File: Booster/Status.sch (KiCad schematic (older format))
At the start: 41 parts

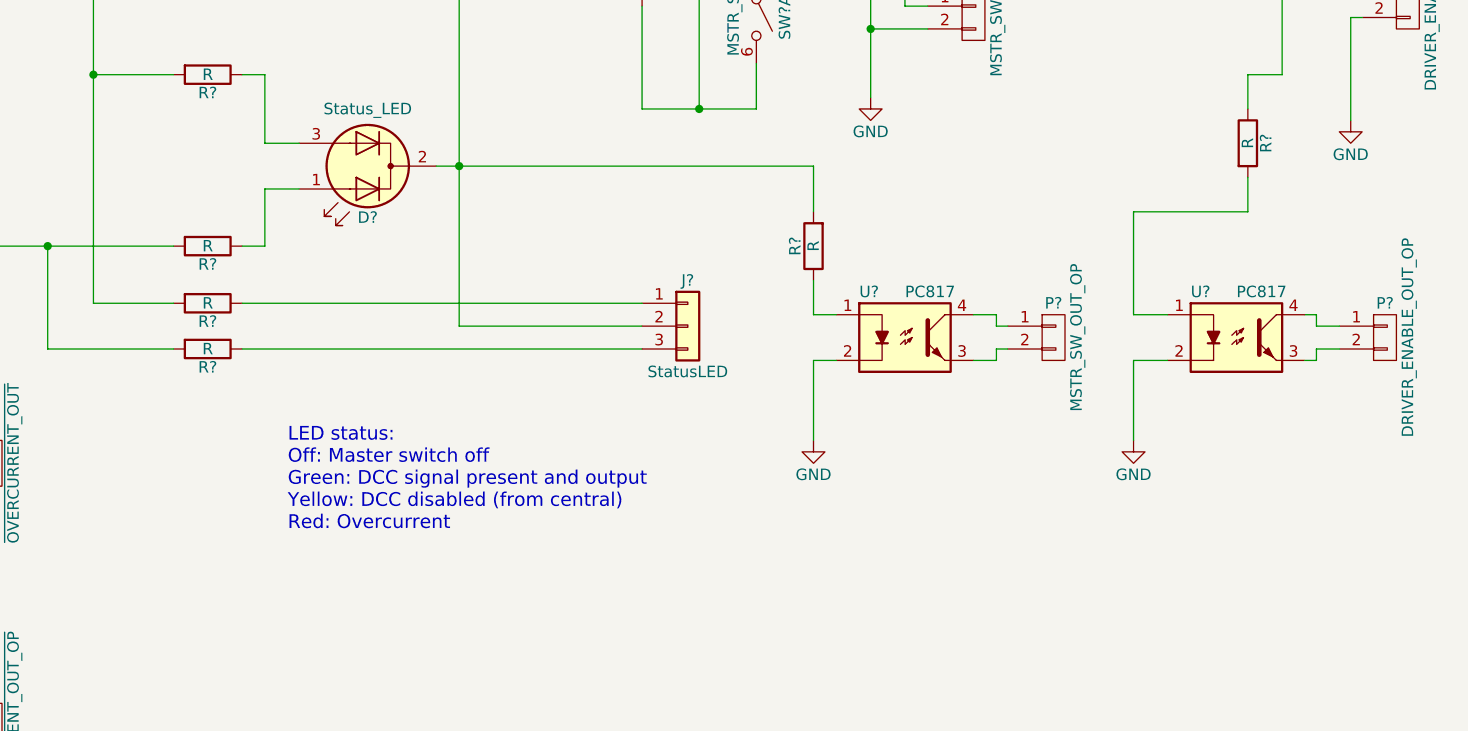
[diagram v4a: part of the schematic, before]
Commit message: Reset overcurrent timeout now linked to the master switch, not the input signal.
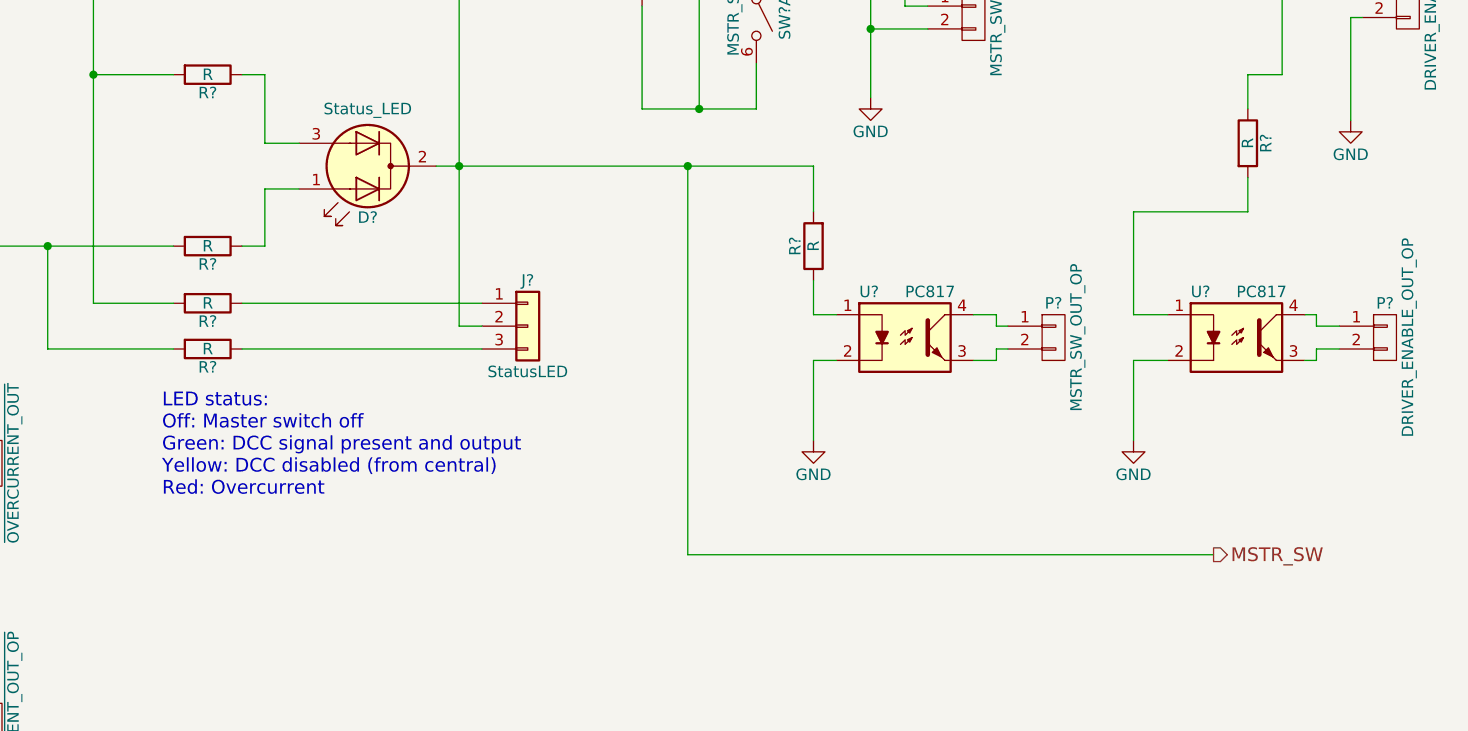
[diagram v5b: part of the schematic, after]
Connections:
- net MSTR_SW: now reaches D?.2 (K), J?.2 (Pin_2), P?.1 (P1), P?.1 (P1), R?.2, R?.2, SW?.1 (A), U?.13
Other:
- moved on the sheet: J?
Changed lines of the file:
@@
 Text HLabel 10250 2050 2    60   Output ~ 0
 DRIVER_ENABLE
-Text Notes 6050 5950 0    60   ~ 0
+Text Notes 5500 5800 0    60   ~ 0
 LED status:\nOff: Master switch off\nGreen: DCC signal present and output\nYellow: DCC disabled (from central)\nRed: Overcurrent
 $Comp
@@
 L Conn_01x03 J?
 U 1 1 5A0BF38D
-P 7800 5050
-F 0 "J?" H 7800 5250 50  0000 C CNN
-F 1 "StatusLED" H 7800 4850 50  0000 C CNN
-F 2 "" H 7800 5050 50  0001 C CNN
-F 3 "" H 7800 5050 50  0001 C CNN
-	1    7800 5050
+P 7100 5050
+F 0 "J?" H 7100 5250 50  0000 C CNN
+F 1 "StatusLED" H 7100 4850 50  0000 C CNN
+F 2 "" H 7100 5050 50  0001 C CNN
+F 3 "" H 7100 5050 50  0001 C CNN
+	1    7100 5050
 	1    0    0    -1
 $EndComp
@@
 	6700 4350 8350 4350
 Wire Wire Line
-	6800 5050 7600 5050
+	6800 5050 6900 5050
 Connection ~ 6800 4350
 Wire Wire Line
-	7600 4950 5850 4950
-Wire Wire Line
-	5850 5150 7600 5150
+	6900 4950 5850 4950
+Wire Wire Line
+	5850 5150 6900 5150
 Wire Wire Line
 	8100 3150 8100 3500
@@
 Text Notes 2300 3950 0    60   ~ 0
 Acting as inverter
+Wire Wire Line
+	7800 4350 7800 6050
+Wire Wire Line
+	7800 6050 10100 6050
+Connection ~ 7800 4350
+Text HLabel 10100 6050 2    60   Output ~ 0
+MSTR_SW
 $EndSCHEMATC

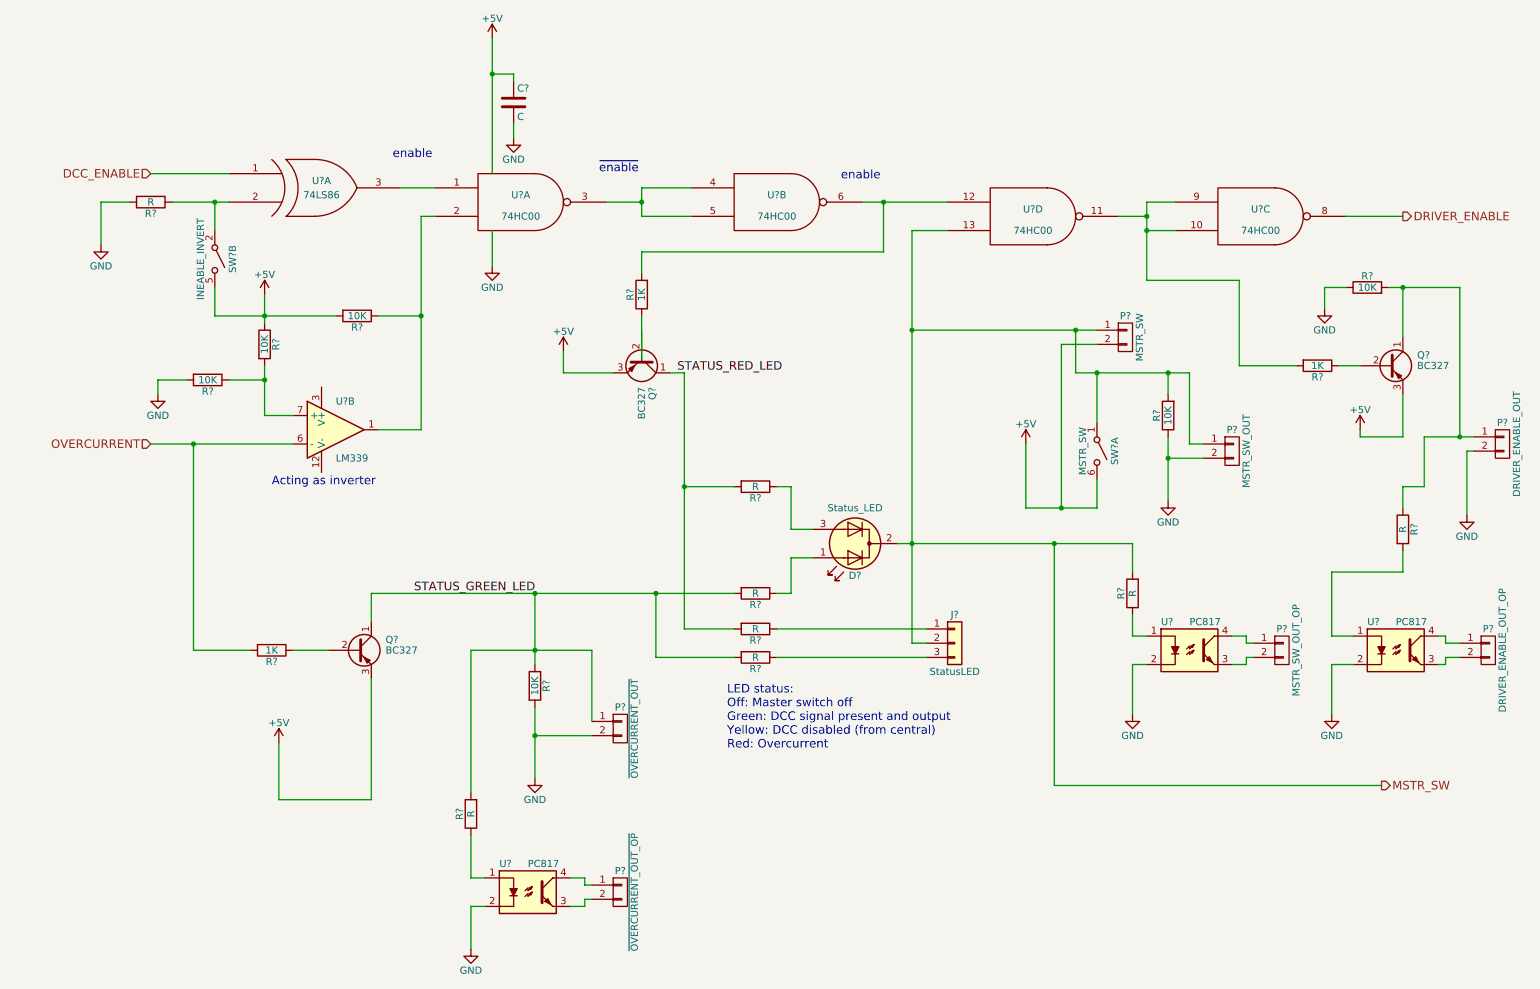
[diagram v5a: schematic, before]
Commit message: Removed need for enable signal replacing it with a missing pulse detection RC based circuit.
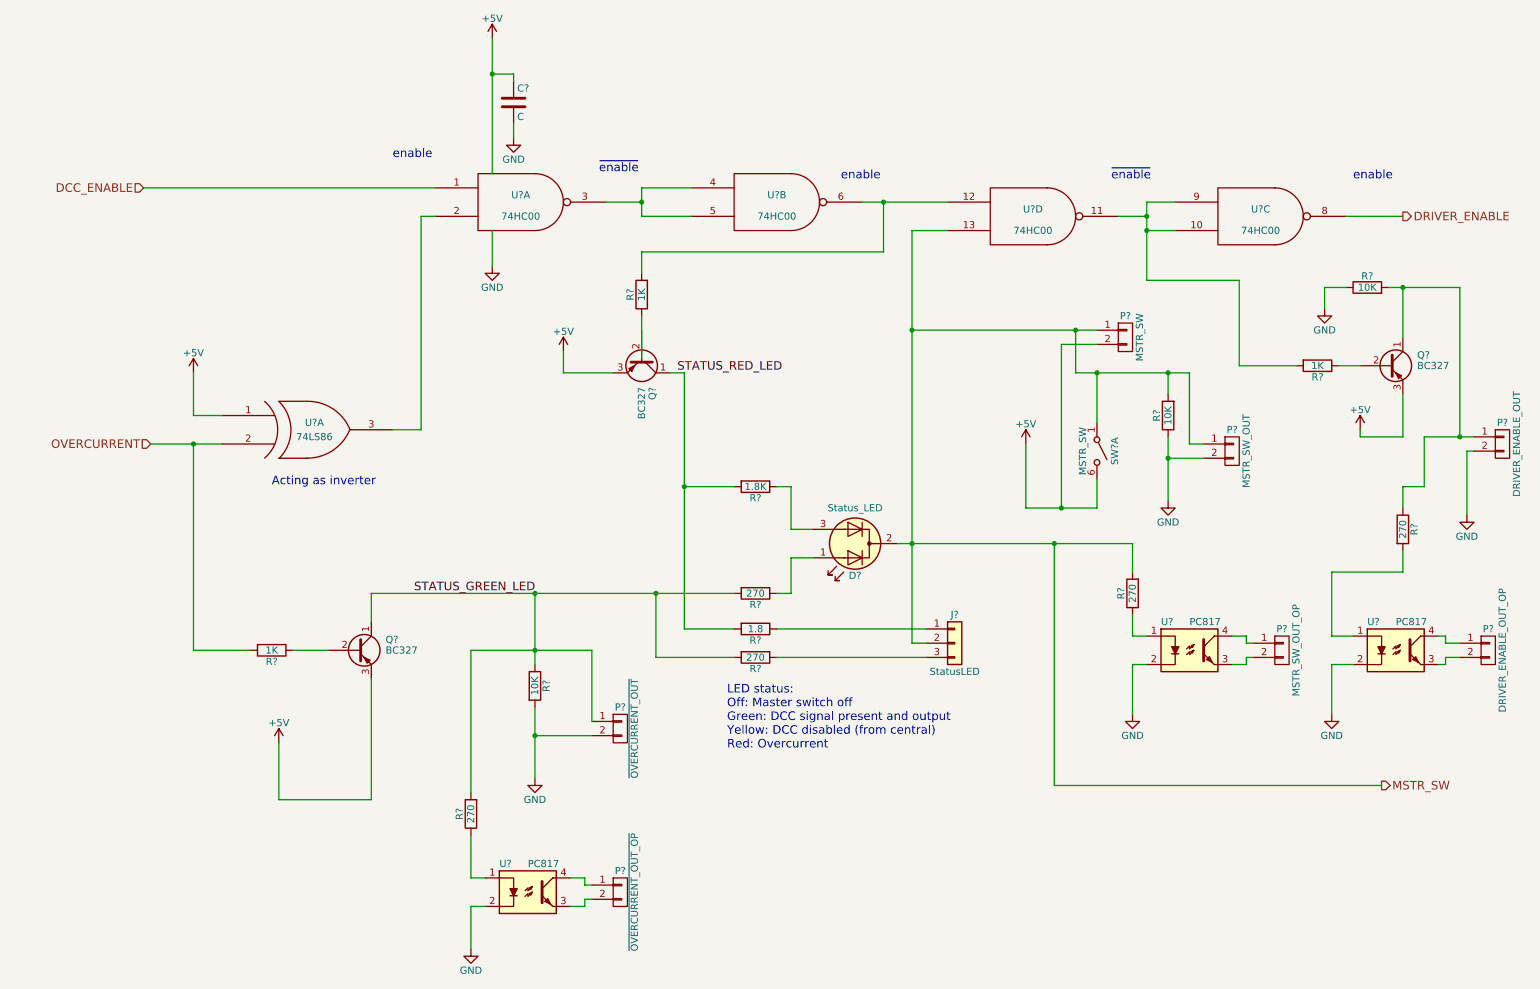
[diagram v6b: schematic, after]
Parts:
- removed R?: R, symbol R
- removed R? (x3): 10K, symbol R
- removed SW?: INEABLE_INVERT, symbol SW_SPST_x03
- removed U?: LM339, symbol LM339
- R? (x5): value R -> 270
- R?: value R -> 1.8K
- R?: value R -> 1.8
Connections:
- net +5V: now also U?.1 (IN1)
- net DCC_ENABLE: now also U?.1; no longer U?.1 (IN1)
- net OVERCURRENT: now also U?.2 (IN2)
- net at U?.3 (OUT): now also U?.2; no longer U?.1
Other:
- moved on the sheet: U?A
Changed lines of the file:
@@
 Comment4 ""
 $EndDescr
-Text HLabel 1450 1750 0    60   Input ~ 0
+Text HLabel 1400 1850 0    60   Input ~ 0
 DCC_ENABLE
 Text HLabel 1450 3650 0    60   Input ~ 0
@@
 P 5700 4700
 F 0 "R?" V 5780 4700 50  0000 C CNN
-F 1 "R" V 5700 4700 50  0000 C CNN
+F 1 "270" V 5700 4700 50  0000 C CNN
 F 2 "" V 5630 4700 50  0001 C CNN
 F 3 "" H 5700 4700 50  0001 C CNN
@@
 P 5700 3950
 F 0 "R?" V 5780 3950 50  0000 C CNN
-F 1 "R" V 5700 3950 50  0000 C CNN
+F 1 "1.8K" V 5700 3950 50  0000 C CNN
 F 2 "" V 5630 3950 50  0001 C CNN
 F 3 "" H 5700 3950 50  0001 C CNN
@@
 P 5700 4950
 F 0 "R?" V 5780 4950 50  0000 C CNN
-F 1 "R" V 5700 4950 50  0000 C CNN
+F 1 "1.8" V 5700 4950 50  0000 C CNN
 F 2 "" V 5630 4950 50  0001 C CNN
 F 3 "" H 5700 4950 50  0001 C CNN
@@
 P 5700 5150
 F 0 "R?" V 5780 5150 50  0000 C CNN
-F 1 "R" V 5700 5150 50  0000 C CNN
+F 1 "270" V 5700 5150 50  0000 C CNN
 F 2 "" V 5630 5150 50  0001 C CNN
 F 3 "" H 5700 5150 50  0001 C CNN
@@
 P 10250 4250
 F 0 "R?" V 10330 4250 50  0000 C CNN
-F 1 "R" V 10250 4250 50  0000 C CNN
+F 1 "270" V 10250 4250 50  0000 C CNN
 F 2 "" V 10180 4250 50  0001 C CNN
 F 3 "" H 10250 4250 50  0001 C CNN
@@
 P 8350 4700
 F 0 "R?" V 8430 4700 50  0000 C CNN
-F 1 "R" V 8350 4700 50  0000 C CNN
+F 1 "270" V 8350 4700 50  0000 C CNN
 F 2 "" V 8280 4700 50  0001 C CNN
 F 3 "" H 8350 4700 50  0001 C CNN
@@
 P 3700 6250
 F 0 "R?" V 3780 6250 50  0000 C CNN
-F 1 "R" V 3700 6250 50  0000 C CNN
+F 1 "270" V 3700 6250 50  0000 C CNN
 F 2 "" V 3630 6250 50  0001 C CNN
 F 3 "" H 3700 6250 50  0001 C CNN
@@
 L 74LS86 U?
 U 1 1 5A0F5EBC
-P 2600 1850
-F 0 "U?" H 2650 1900 50  0000 C CNN
-F 1 "74LS86" H 2650 1800 50  0000 C CNN
-F 2 "" H 2600 1850 50  0001 C CNN
-F 3 "" H 2600 1850 50  0001 C CNN
-	1    2600 1850
+P 2550 3550
+F 0 "U?" H 2600 3600 50  0000 C CNN
+F 1 "74LS86" H 2600 3500 50  0000 C CNN
+F 2 "" H 2550 3550 50  0001 C CNN
+F 3 "" H 2550 3550 50  0001 C CNN
+	1    2550 3550
 	1    0    0    -1
 $EndComp
@@
 $EndComp
 $Comp
-L SW_SPST_x03 SW?
-U 2 1 5A1166C8
-P 1900 2350
-F 0 "SW?" H 1900 2475 50  0000 C CNN
-F 1 "INEABLE_INVERT" H 1900 2250 50  0000 C CNN
-F 2 "" H 1900 2350 50  0001 C CNN
-F 3 "" H 1900 2350 50  0001 C CNN
-	2    1900 2350
-	0    1    1    0
-$EndComp
-$Comp
-L GND #PWR?
-U 1 1 5A116829
-P 1100 2250
-F 0 "#PWR?" H 1100 2000 50  0001 C CNN
-F 1 "GND" H 1100 2100 50  0000 C CNN
-F 2 "" H 1100 2250 50  0001 C CNN
-F 3 "" H 1100 2250 50  0001 C CNN
-	1    1100 2250
-	1    0    0    -1
-$EndComp
-$Comp
-L R R?
-U 1 1 5A116A16
-P 1450 1950
-F 0 "R?" V 1530 1950 50  0000 C CNN
-F 1 "R" V 1450 1950 50  0000 C CNN
-F 2 "" V 1380 1950 50  0001 C CNN
-F 3 "" H 1450 1950 50  0001 C CNN
-	1    1450 1950
-	0    1    1    0
-$EndComp
-$Comp
-L +5V #PWR?
-U 1 1 5A116BBB
-P 2250 2600
-F 0 "#PWR?" H 2250 2450 50  0001 C CNN
-F 1 "+5V" H 2250 2740 50  0000 C CNN
-F 2 "" H 2250 2600 50  0001 C CNN
-F 3 "" H 2250 2600 50  0001 C CNN
-	1    2250 2600
-	1    0    0    -1
-$EndComp
-$Comp
 L 74HC00 U?
 U 2 1 5A11F087
@@
 $EndComp
 Wire Wire Line
-	1450 1750 2000 1750
-Wire Wire Line
 	1750 3650 1750 5100
 Wire Wire Line
@@
 	3350 2050 3450 2050
 Wire Wire Line
-	3200 1850 3450 1850
-Wire Wire Line
 	4650 1950 4900 1950
 Wire Wire Line
@@
 	9850 2050 10250 2050
 Wire Wire Line
-	1600 1950 2000 1950
-Wire Wire Line
-	1300 1950 1100 1950
-Wire Wire Line
-	1100 1950 1100 2250
-Wire Wire Line
-	1900 2150 1900 1950
-Connection ~ 1900 1950
-Wire Wire Line
-	1900 2550 1900 2750
-Wire Wire Line
-	1900 2750 2750 2750
-Wire Wire Line
-	2250 2600 2250 2800
-Wire Wire Line
 	3850 2150 3850 2400
 Wire Wire Line
@@
 	6600 2300 6600 1950
 Connection ~ 6600 1950
-$Comp
-L LM339 U?
-U 2 1 5A375C9A
-P 2750 3550
-F 0 "U?" H 2750 3750 50  0000 L CNN
-F 1 "LM339" H 2750 3350 50  0000 L CNN
-F 2 "" H 2700 3650 50  0000 C CNN
-F 3 "" H 2800 3750 50  0000 C CNN
-	2    2750 3550
-	1    0    0    -1
-$EndComp
-Wire Wire Line
-	1450 3650 2450 3650
-Wire Wire Line
-	2250 3450 2450 3450
-Wire Wire Line
-	2250 3100 2250 3450
-Wire Wire Line
-	2000 3200 2250 3200
-$Comp
-L R R?
-U 1 1 5A376953
-P 2250 2950
-F 0 "R?" V 2330 2950 50  0000 C CNN
-F 1 "10K" V 2250 2950 50  0000 C CNN
-F 2 "" V 2180 2950 50  0000 C CNN
-F 3 "" H 2250 2950 50  0000 C CNN
-	1    2250 2950
-	1    0    0    -1
-$EndComp
-Connection ~ 2250 3200
-Connection ~ 2250 2750
-$Comp
-L R R?
-U 1 1 5A376D88
-P 1850 3200
-F 0 "R?" V 1930 3200 50  0000 C CNN
-F 1 "10K" V 1850 3200 50  0000 C CNN
-F 2 "" V 1780 3200 50  0000 C CNN
-F 3 "" H 1850 3200 50  0000 C CNN
-	1    1850 3200
-	0    1    1    0
-$EndComp
-Wire Wire Line
-	1700 3200 1500 3200
-Wire Wire Line
-	1500 3200 1500 3300
-$Comp
-L GND #PWR?
-U 1 1 5A376ECE
-P 1500 3300
-F 0 "#PWR?" H 1500 3050 50  0001 C CNN
-F 1 "GND" H 1500 3150 50  0000 C CNN
-F 2 "" H 1500 3300 50  0000 C CNN
-F 3 "" H 1500 3300 50  0000 C CNN
-	1    1500 3300
-	1    0    0    -1
-$EndComp
-Wire Wire Line
-	3350 3550 3050 3550
-$Comp
-L R R?
-U 1 1 5A377144
-P 2900 2750
-F 0 "R?" V 2980 2750 50  0000 C CNN
-F 1 "10K" V 2900 2750 50  0000 C CNN
-F 2 "" V 2830 2750 50  0000 C CNN
-F 3 "" H 2900 2750 50  0000 C CNN
-	1    2900 2750
-	0    1    1    0
-$EndComp
-Wire Wire Line
-	3050 2750 3350 2750
-Connection ~ 3350 2750
+Wire Wire Line
+	1450 3650 1950 3650
+Wire Wire Line
+	3350 3550 3150 3550
 Text Notes 2300 3950 0    60   ~ 0
 Acting as inverter
@@
 Text HLabel 10100 6050 2    60   Output ~ 0
 MSTR_SW
+Wire Wire Line
+	1950 3450 1750 3450
+Wire Wire Line
+	1750 3450 1750 3150
+$Comp
+L +5V #PWR?
+U 1 1 5A390297
+P 1750 3150
+F 0 "#PWR?" H 1750 3000 50  0001 C CNN
+F 1 "+5V" H 1750 3290 50  0000 C CNN
+F 2 "" H 1750 3150 50  0000 C CNN
+F 3 "" H 1750 3150 50  0000 C CNN
+	1    1750 3150
+	1    0    0    -1
+$EndComp
+Wire Wire Line
+	1400 1850 3450 1850
+Text Notes 8200 1800 0    60   ~ 0
+~enable
+Text Notes 9900 1800 0    60   ~ 0
+enable
 $EndSCHEMATC
